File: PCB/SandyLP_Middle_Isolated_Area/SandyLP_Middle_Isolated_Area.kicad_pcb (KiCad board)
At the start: 2 copper layers, 47.1 x 18.5 mm, 42 parts

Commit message: ネジ位置変更
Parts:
- moved H2 7.62 mm to (29.4, 49.6)
- moved H1 5.32 mm to (29.4, 41.3)
- moved H3 2.38 mm to (49.6, 41.3)
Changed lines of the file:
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@@
 		(fp_arc
 			(start 95.805 -16.764254)
-			(mid 96.39077 -18.178497)
+			(mid 96.390776 -18.178462)
 			(end 97.805 -18.764254)
 			(stroke
@@
 		(fp_arc
 			(start 140.485 -18.764254)
-			(mid 141.899197 -18.178465)
+			(mid 141.899233 -18.178471)
 			(end 142.485 -16.764254)
 			(stroke
@@
 		(fp_arc
 			(start 142.475 -2.628468)
-			(mid 141.889202 -1.214275)
+			(mid 141.889208 -1.21424)
 			(end 140.475 -0.628468)
 			(stroke
@@
 	(footprint "locallib:MountingHole_1.8-2.2mm_M2_Pad_minimal"
 		(layer "F.Cu")
-		(at 24.63031 55.578405)
+		(at 29.39281 49.62528)
 		(descr "Mounting Hole 2.2mm, M2")
 		(tags "mounting hole 2.2mm m2")
@@
 	(footprint "locallib:MountingHole_1.8-2.2mm_M2_Pad_minimal"
 		(layer "F.Cu")
-		(at 49.633435 43.672155 180)
+		(at 49.633435 41.290905 180)
 		(descr "Mounting Hole 2.2mm, M2")
 		(tags "mounting hole 2.2mm m2")
@@
 	(footprint "locallib:MountingHole_1.8-2.2mm_M2_Pad_minimal"
 		(layer "F.Cu")
-		(at 24.63031 43.672155 180)
+		(at 29.39281 41.290905 180)
 		(descr "Mounting Hole 2.2mm, M2")
 		(tags "mounting hole 2.2mm m2")
@@
 		(fp_arc
 			(start 0.325 1.05)
-			(mid -0.050512 2.285658)
+			(mid -0.050512 2.285659)
 			(end -1.332701 2.440097)
 			(stroke
@@
 		(fp_arc
 			(start 0.325 1.05)
-			(mid -0.050512 2.285658)
+			(mid -0.050512 2.285659)
 			(end -1.332701 2.440097)
 			(stroke
@@
 		(fp_arc
 			(start 0.325 1.05)
-			(mid -0.050512 2.285658)
+			(mid -0.050512 2.285659)
 			(end -1.332701 2.440097)
 			(stroke
@@
 		(fp_arc
 			(start 0.325 1.05)
-			(mid -0.050512 2.285658)
+			(mid -0.050512 2.285659)
 			(end -1.332701 2.440097)
 			(stroke
@@
 		(fp_arc
 			(start 0.325 1.05)
-			(mid -0.050512 2.285658)
+			(mid -0.050512 2.285659)
 			(end -1.332701 2.440097)
 			(stroke
@@
 		(fp_arc
 			(start 0.325 1.05)
-			(mid -0.050512 2.285658)
+			(mid -0.050512 2.285659)
 			(end -1.332701 2.440097)
 			(stroke
@@
 		(fp_arc
 			(start 0.325 1.05)
-			(mid -0.050512 2.285658)
+			(mid -0.050512 2.285659)
 			(end -1.332701 2.440097)
 			(stroke
@@
 		(fp_arc
 			(start 0.325 1.05)
-			(mid -0.050511 2.285658)
+			(mid -0.050512 2.285658)
 			(end -1.332701 2.440097)
 			(stroke
@@
 		(min_thickness 0.254)
 		(filled_areas_thickness no)
-		(fill yes
+		(fill
 			(thermal_gap 0.508)
 			(thermal_bridge_width 0.508)
@@
 		(polygon
 			(pts
-				(xy 306.808435 97.25028) (xy 21.058435 97.25028) (xy 21.058435 21.05028) (xy 306.808435 21.05028)
+				(xy 306.808435 97.25028) (xy 13.914685 97.25028) (xy 13.914685 21.05028) (xy 306.808435 21.05028)
 			)
 		)

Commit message: 基板外形を調整。ネジ位置変更。ゾーンのクリアランス調整。
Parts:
- removed REF** (x6): ICON_Spacer, locallib:ICON_Spacer
- removed REF** (x12): ICON_Screw_Medium, locallib:ICON_Screw_Medium
- removed REF** (x8): ICON_Nut & Washer, locallib:ICON_Nut & Washer
- H1, H2, H3, H4: footprint locallib:MountingHole_1.8-2.2mm_M2_Pad_minimal -> locallib:MountingHole_2.2mm_M2_Pad_minimal; moved to B.Cu
- moved Cutout1 95.2 mm to (68.7, 59.2)
- moved T_C0/C6 23.8 mm to (49.6, 42.5)
- moved H3 16.1 mm to (65.8, 40.7), turned to 0 degrees
- moved H2 6.67 mm to (28.7, 56.3), turned to 180 degrees
- moved H1 0.97 mm to (28.7, 40.7), turned to 0 degrees
- turned H4 to 180 degrees
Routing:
- added copper zone on B.Cu, net GND
- added copper zone on F.Cu, net GND
- removed copper zone on B.Cu, net (none)
- removed copper zone on F.Cu, net (none)
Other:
- board size 47.1 x 18.5 mm -> 42.3 x 20.8 mm

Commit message: USBコネクタ周りの配線に合わせて、Mid孤立部分のネジへのピン割り当てを変更。
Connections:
- H2 pad 1: GND -> Mid_row4
- H4 pad 1: Mid_row4 -> GND
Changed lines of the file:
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@@
 			(layers "*.Cu" "*.Mask")
 			(remove_unused_layers no)
-			(net 5 "Mid_row4")
+			(net 8 "GND")
 			(pinfunction "1")
 			(pintype "input")
@@
 			(layers "*.Cu" "*.Mask")
 			(remove_unused_layers no)
-			(net 8 "GND")
+			(net 5 "Mid_row4")
 			(pinfunction "1")
 			(pintype "input")

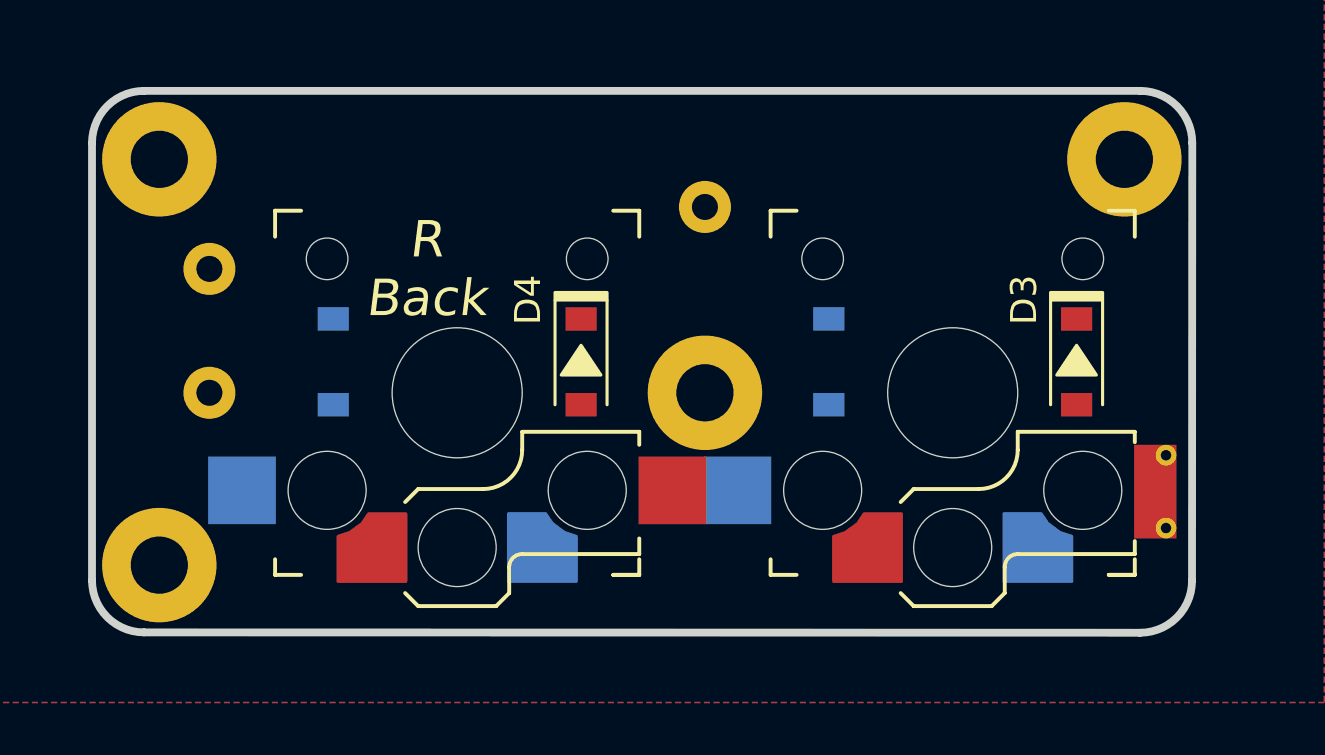
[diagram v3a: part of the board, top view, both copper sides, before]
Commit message: 配線完了。ビア打ちまだ。
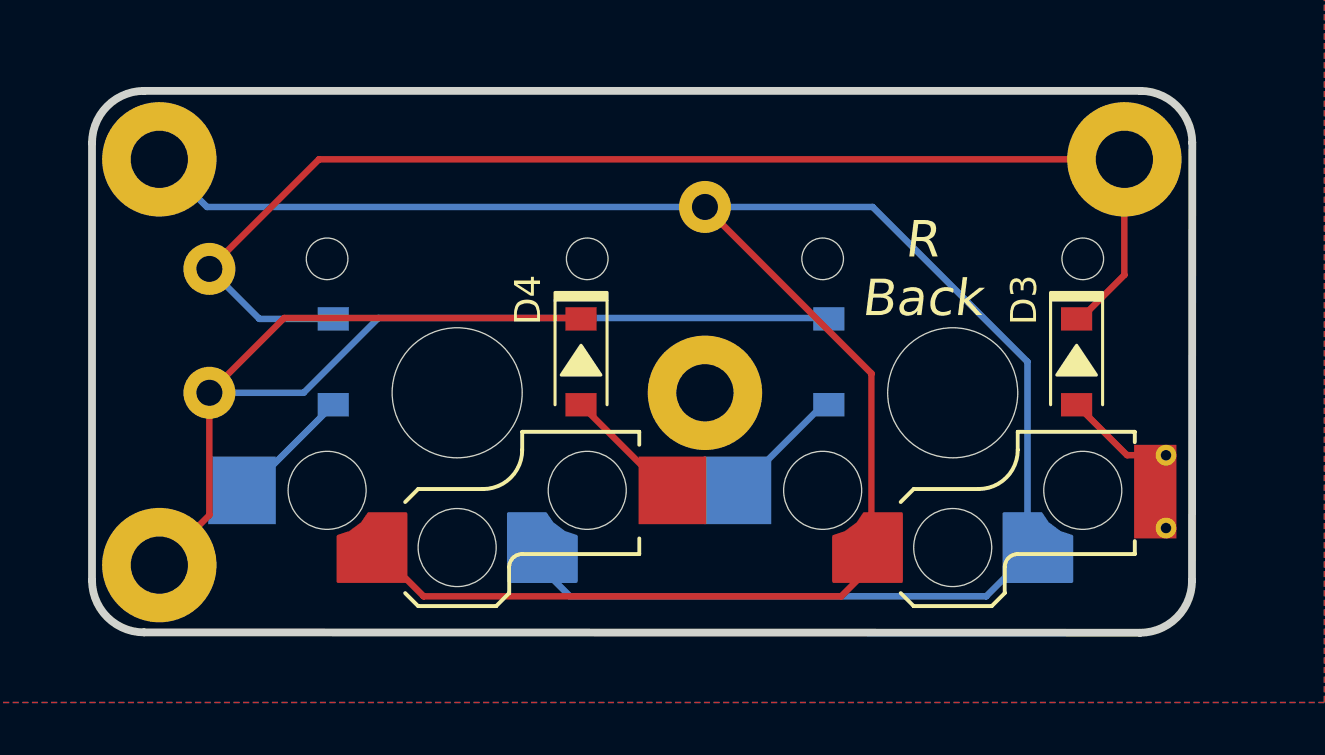
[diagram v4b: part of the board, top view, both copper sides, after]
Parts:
- turned T_R0 to 0 degrees
- turned T_R4 to 0 degrees
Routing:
- net Mid_col0/6: track 0.00 -> 101.0 mm
- net Mid_row0: track 0.00 -> 49.5 mm
- net Mid_row4: track 0.00 -> 47.9 mm
- net Net-(D2-A): track 0.00 -> 4.88 mm
- net Net-(D4-A): track 0.00 -> 4.88 mm
- net Net-(D1-A): track 0.00 -> 4.88 mm
- net Net-(D3-A): track 0.00 -> 4.24 mm

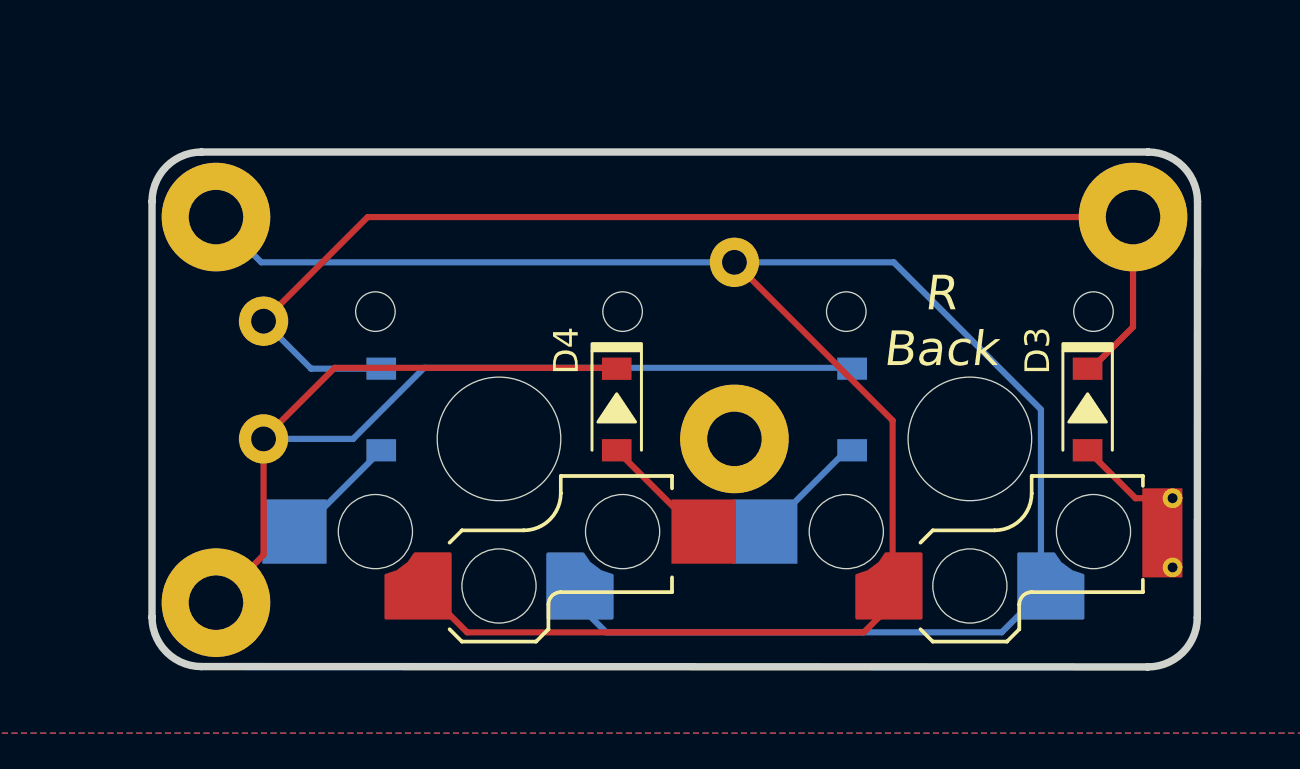
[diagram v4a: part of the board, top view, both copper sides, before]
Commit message: 外形のコーナーを緩く。
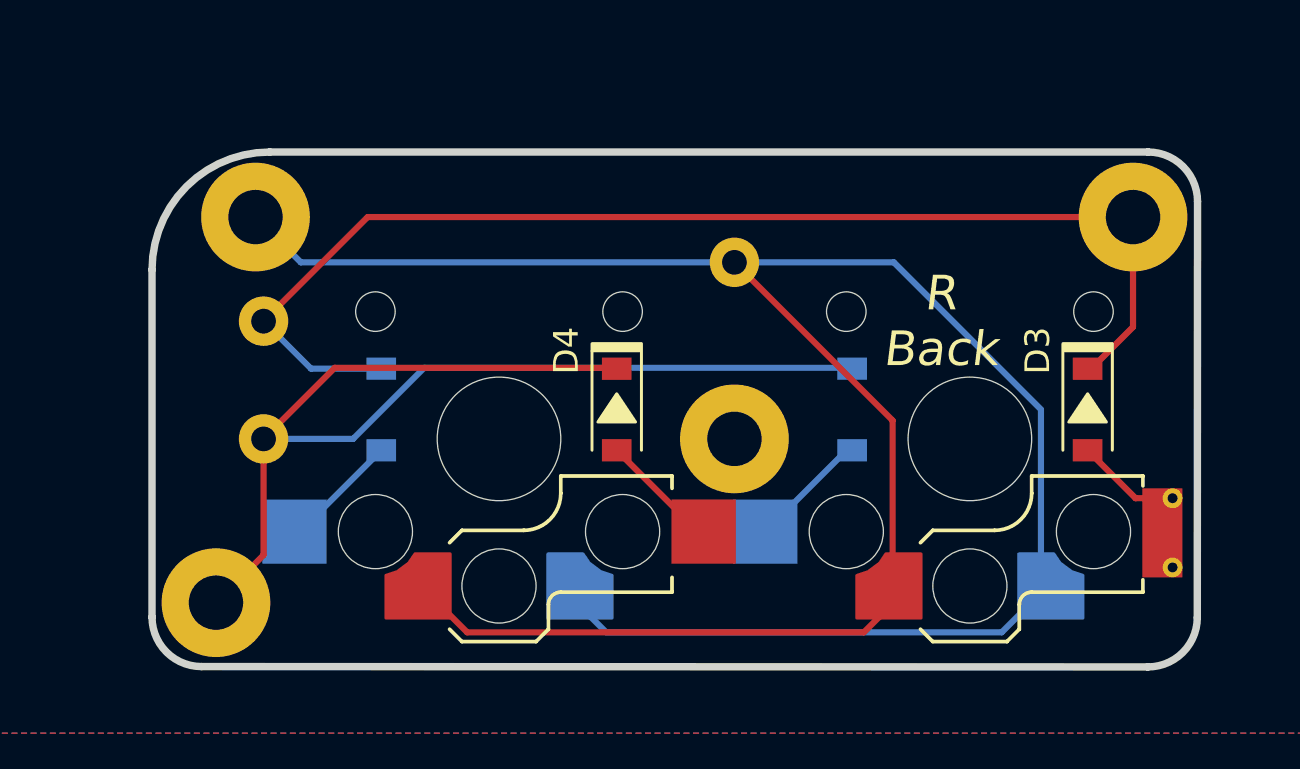
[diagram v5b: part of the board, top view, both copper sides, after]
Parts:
- Cutout1: footprint locallib:SandyLP_outline_Mid_Isolated_Area -> locallib:SandyLP_outline_Mid_Isolated_Area_gentle_corner
- moved H1 1.60 mm to (30.3, 40.7)
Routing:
- net Mid_col0/6: track 101.0 -> 99.4 mm
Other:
- outline, holes or cut-outs redrawn
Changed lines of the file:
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@@
 		(allow_soldermask_bridges_in_footprints no)
 		(aux_axis_origin 21.058435 21.05028)
-		(grid_origin 21.058435 40.10028)
+		(grid_origin 28.658435 56.25028)
 		(pcbplotparams
 			(layerselection 0x00310fc_ffffffff)
@@
 		)
 	)
-	(footprint "locallib:SandyLP_outline_Mid_Isolated_Area"
+	(footprint "locallib:SandyLP_outline_Mid_Isolated_Area_gentle_corner"
 		(locked yes)
 		(layer "F.Cu")
@@
 			)
 		)
-		(property "Footprint" "locallib:SandyLP_outline_Mid_Isolated_Area"
+		(property "Footprint" "locallib:SandyLP_outline_Mid_Isolated_Area_gentle_corner"
 			(at 0 0 0)
 			(layer "F.Fab")
@@
 			)
 		)
-		(attr through_hole board_only)
+		(attr through_hole board_only exclude_from_pos_files exclude_from_bom)
 		(fp_line
 			(start -47.625 -38.1)
@@
 		(fp_line
 			(start -42.6125 -2.314214)
-			(end -42.6125 -19.13129)
+			(end -42.6125 -16.36879)
 			(stroke
 				(width 0.3)
@@
 		)
 		(fp_line
-			(start -40.6125 -21.13129)
-			(end -2.315 -21.13129)
+			(start -40.6125 -0.314214)
+			(end -2.325 -0.3)
 			(stroke
 				(width 0.3)
@@
 		)
 		(fp_line
-			(start -40.6125 -0.314214)
-			(end -2.325 -0.3)
+			(start -37.85 -21.13129)
+			(end -2.315 -21.13129)
 			(stroke
 				(width 0.3)
@@
 		)
 		(fp_arc
-			(start -42.6125 -19.13129)
-			(mid -42.026714 -20.545504)
-			(end -40.6125 -21.13129)
+			(start -42.6125 -16.36879)
+			(mid -41.217596 -19.736386)
+			(end -37.85 -21.13129)
 			(stroke
 				(width 0.3)
-				(type solid)
+				(type default)
 			)
 			(layer "Edge.Cuts")
@@
 	(footprint "locallib:MountingHole_2.2mm_M2_Pad_minimal"
 		(layer "B.Cu")
-		(at 28.658435 40.65028)
+		(at 30.258435 40.65028)
 		(descr "Mounting Hole 2.2mm, M2")
 		(tags "mounting hole 2.2mm m2")
@@
 		)
 		(property "Value" "Conn_01x01"
-			(at 0 -2.05 360)
+			(at 0 -2.05 0)
 			(layer "B.Fab")
 			(effects
@@
 		)
 		(fp_text user "${REFERENCE}"
-			(at 0 2 360)
+			(at 0 2 0)
 			(layer "B.Fab")
 			(effects
@@
 		)
 		(property "Value" "Conn_01x01"
-			(at 0 -2.05 360)
+			(at 0 -2.05 0)
 			(layer "B.Fab")
 			(effects
@@
 		)
 		(fp_text user "${REFERENCE}"
-			(at 0 2 360)
+			(at 0 2 0)
 			(layer "B.Fab")
 			(effects
@@
 	)
 	(gr_text "#SandyLP_kbd DN0010\nMid-Iso by @jpskenn"
-		(at 48.44281 42.10028 0)
+		(at 49.658435 40.05028 0)
 		(layer "B.SilkS")
 		(effects
@@
 	)
 	(segment
-		(start 30.489685 42.48153)
-		(end 28.658435 40.65028)
+		(start 32.089685 42.48153)
+		(end 30.258435 40.65028)
 		(width 0.25)
 		(layer "B.Cu")
@@
 	)
 	(segment
-		(start 49.633435 42.48153)
-		(end 30.489685 42.48153)
+		(start 60.445935 57.45028)
+		(end 61.970935 55.92528)
 		(width 0.25)
 		(layer "B.Cu")
@@
 	)
 	(segment
-		(start 60.445935 57.45028)
-		(end 61.970935 55.92528)
+		(start 62.033435 48.434416)
+		(end 62.033435 55.86278)
 		(width 0.25)
 		(layer "B.Cu")
@@
 	)
 	(segment
-		(start 62.033435 48.434416)
-		(end 62.033435 55.86278)
+		(start 49.633435 42.48153)
+		(end 32.089685 42.48153)
 		(width 0.25)
 		(layer "B.Cu")

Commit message: ネジ穴のアイコンを更新
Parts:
- added REF**: ICON_Screw_Long_Medium, locallib:ICON_Screw_Long_Medium, F.Cu at (48.9, 41.0)
- added REF**: ICON_Nut & Washer, locallib:ICON_Nut & Washer, F.Cu at (58.2, 40.6)
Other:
- board text added: "Back="
- board text added: "Front="

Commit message: ビア打ち
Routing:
- net Mid_row4: track 47.9 -> 49.3 mm
- net GND: vias 0 -> 18
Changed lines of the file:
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@@
 		(fp_arc
 			(start 0.582958 -5.961016)
-			(mid 0.542326 -6.113994)
+			(mid 0.542323 -6.113993)
 			(end 0.665318 -6.21362)
 			(stroke
@@
 		(fp_arc
 			(start 2.475824 -5.107131)
-			(mid 1.399999 -5.299999)
+			(mid 1.4 -5.3)
 			(end 0.555319 -5.993622)
 			(stroke
@@
 		(fp_arc
 			(start 0.671822 -3.333526)
-			(mid 0.262251 -3.449502)
+			(mid 0.262246 -3.449501)
 			(end 0.25 -3.875)
 			(stroke
@@
 	)
 	(segment
-		(start 54.870935 57.45028)
+		(start 37.295935 55.92528)
+		(end 38.820935 57.45028)
+		(width 0.25)
+		(layer "F.Cu")
+		(net 3)
+	)
+	(segment
+		(start 49.633435 42.48153)
+		(end 54.583435 47.43153)
+		(width 0.25)
+		(layer "F.Cu")
+		(net 3)
+	)
+	(segment
+		(start 40.952185 57.45028)
+		(end 42.083435 56.31903)
+		(width 0.25)
+		(layer "F.Cu")
+		(net 3)
+	)
+	(segment
+		(start 54.583435 51.11903)
+		(end 56.033435 52.56903)
+		(width 0.25)
+		(layer "F.Cu")
+		(net 3)
+	)
+	(segment
+		(start 56.033435 55.63778)
 		(end 56.358435 55.96278)
 		(width 0.25)
@@
 	)
 	(segment
-		(start 56.033435 48.88153)
-		(end 56.033435 55.63778)
+		(start 56.002185 56.31903)
+		(end 56.358435 55.96278)
 		(width 0.25)
 		(layer "F.Cu")
@@
 	)
 	(segment
-		(start 49.633435 42.48153)
-		(end 56.033435 48.88153)
+		(start 42.083435 56.31903)
+		(end 56.002185 56.31903)
 		(width 0.25)
 		(layer "F.Cu")
@@
 	)
 	(segment
-		(start 37.295935 55.92528)
-		(end 38.820935 57.45028)
+		(start 54.583435 47.43153)
+		(end 54.583435 51.11903)
 		(width 0.25)
 		(layer "F.Cu")
@@
 	(segment
 		(start 38.820935 57.45028)
-		(end 54.870935 57.45028)
+		(end 40.952185 57.45028)
 		(width 0.25)
 		(layer "F.Cu")
@@
 	)
 	(segment
-		(start 56.033435 55.63778)
-		(end 56.358435 55.96278)
+		(start 56.033435 52.56903)
+		(end 56.033435 55.63778)
 		(width 0.25)
 		(layer "F.Cu")
@@
 	(segment
 		(start 42.920935 55.92528)
-		(end 44.445935 57.45028)
+		(end 43.314685 56.31903)
+		(width 0.25)
+		(layer "B.Cu")
+		(net 3)
+	)
+	(segment
+		(start 57.250535 56.31903)
+		(end 58.381785 57.45028)
 		(width 0.25)
 		(layer "B.Cu")
@@
 	)
 	(segment
-		(start 44.445935 57.45028)
+		(start 58.381785 57.45028)
 		(end 60.445935 57.45028)
 		(width 0.25)
@@
 	)
 	(segment
+		(start 43.314685 56.31903)
+		(end 57.250535 56.31903)
+		(width 0.25)
+		(layer "B.Cu")
+		(net 3)
+	)
+	(segment
 		(start 67.358435 52.02528)
 		(end 65.86156 52.02528)
@@
 	)
 	(segment
-		(start 44.83656 46.75028)
-		(end 37.052185 46.75028)
+		(start 34.177185 49.62528)
+		(end 30.583435 49.62528)
 		(width 0.25)
 		(layer "F.Cu")
@@
 	)
 	(segment
-		(start 37.052185 46.75028)
-		(end 34.177185 49.62528)
+		(start 30.583435 54.32528)
+		(end 30.583435 49.62528)
 		(width 0.25)
 		(layer "F.Cu")
@@
 	)
 	(segment
-		(start 30.583435 54.32528)
-		(end 30.583435 49.62528)
+		(start 44.870935 46.784655)
+		(end 44.00531 45.91903)
 		(width 0.25)
 		(layer "F.Cu")
@@
 	)
 	(segment
-		(start 34.177185 49.62528)
-		(end 30.583435 49.62528)
+		(start 44.00531 45.91903)
+		(end 37.883435 45.91903)
 		(width 0.25)
 		(layer "F.Cu")
@@
 	)
 	(segment
-		(start 44.870935 46.784655)
-		(end 44.83656 46.75028)
+		(start 37.883435 45.91903)
+		(end 34.177185 49.62528)
 		(width 0.25)
 		(layer "F.Cu")
@@
 	)
 	(segment
-		(start 54.36156 46.75028)
-		(end 37.08031 46.75028)
+		(start 54.395935 46.784655)
+		(end 54.36156 46.75028)
 		(width 0.25)
 		(layer "B.Cu")
@@
 	)
 	(segment
-		(start 54.395935 46.784655)
-		(end 54.36156 46.75028)
+		(start 53.614685 46.75028)
+		(end 52.783435 45.91903)
 		(width 0.25)
 		(layer "B.Cu")
@@
 	)
 	(segment
-		(start 37.08031 46.75028)
+		(start 54.36156 46.75028)
+		(end 53.614685 46.75028)
+		(width 0.25)
+		(layer "B.Cu")
+		(net 5)
+	)
+	(segment
+		(start 37.91156 45.91903)
 		(end 34.20531 49.62528)
 		(width 0.25)
@@
 	)
 	(segment
+		(start 52.783435 45.91903)
+		(end 37.91156 45.91903)
+		(width 0.25)
+		(layer "B.Cu")
+		(net 5)
+	)
+	(segment
 		(start 48.16156 53.37528)
 		(end 44.870935 50.084655)
@@
 		(net 7)
 	)
+	(via
+		(at 32.964655 38.909656)
+		(size 0.8)
+		(drill 0.4)
+		(layers "F.Cu" "B.Cu")
+		(free yes)
+		(net 8)
+	)
+	(via
+		(at 27.011525 41.290908)
+		(size 0.8)
+		(drill 0.4)
+		(layers "F.Cu" "B.Cu")
+		(free yes)
+		(net 8)
+	)
+	(via
+		(at 39.683435 41.51903)
+		(size 0.8)
+		(drill 0.4)
+		(layers "F.Cu" "B.Cu")
+		(free yes)
+		(net 8)
+	)
+	(via
+		(at 67.492809 56.173733)
+		(size 0.8)
+		(drill 0.4)
+		(layers "F.Cu" "B.Cu")
+		(free yes)
+		(net 8)
+	)
+	(via
+		(at 47.252167 38.909656)
+		(size 0.8)
+		(drill 0.4)
+		(layers "F.Cu" "B.Cu")
+		(free yes)
+		(net 8)
+	)
+	(via
+		(at 67.492809 50.815916)
+		(size 0.8)
+		(drill 0.4)
+		(layers "F.Cu" "B.Cu")
+		(free yes)
+		(net 8)
+	)
+	(via
+		(at 27.011525 53.792481)
+		(size 0.8)
+		(drill 0.4)
+		(layers "F.Cu" "B.Cu")
+		(free yes)
+		(net 8)
+	)
+	(via
+		(at 49.633435 57.959655)
+		(size 0.8)
+		(drill 0.4)
+		(layers "F.Cu" "B.Cu")
+		(free yes)
+		(net 8)
+	)
+	(via
+		(at 31.178716 57.959672)
+		(size 0.8)
+		(drill 0.4)
+		(layers "F.Cu" "B.Cu")
+		(free yes)
+		(net 8)
+	)
+	(via
+		(at 46.656854 50.220603)
+		(size 0.8)
+		(drill 0.4)
+		(layers "F.Cu" "B.Cu")
+		(free yes)
+		(net 8)
+	)
+	(via
+		(at 67.492809 43.076847)
+		(size 0.8)
+		(drill 0.4)
+		(layers "F.Cu" "B.Cu")
+		(free yes)
+		(net 8)
+	)
+	(via
+		(at 32.964655 44.862786)
+		(size 0.8)
+		(drill 0.4)
+		(layers "F.Cu" "B.Cu")
+		(free yes)
+		(net 8)
+	)
+	(via
+		(at 63.325618 42.481534)
+		(size 0.8)
+		(drill 0.4)
+		(layers "F.Cu" "B.Cu")
+		(free yes)
+		(net 8)
+	)
+	(via
+		(at 65.70687 57.959672)
+		(size 0.8)
+		(drill 0.4)
+		(layers "F.Cu" "B.Cu")
+		(free yes)
+		(net 8)
+	)
+	(via
+		(at 49.633419 55.41903)
+		(size 0.8)
+		(drill 0.4)
+		(layers "F.Cu" "B.Cu")
+		(free yes)
+		(net 8)
+	)
+	(via
+		(at 53.205297 47.839351)
+		(size 0.8)
+		(drill 0.4)
+		(layers "F.Cu" "B.Cu")
+		(free yes)
+		(net 8)
+	)
+	(via
+		(at 36.536533 51.411229)
+		(size 0.8)
+		(drill 0.4)
+		(layers "F.Cu" "B.Cu")
+		(free yes)
+		(net 8)
+	)
+	(via
+		(at 63.325618 38.909656)
+		(size 0.8)
+		(drill 0.4)
+		(layers "F.Cu" "B.Cu")
+		(free yes)
+		(net 8)
+	)
 	(zone
